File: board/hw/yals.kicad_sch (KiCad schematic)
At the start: 2 parts, among them J2 UART

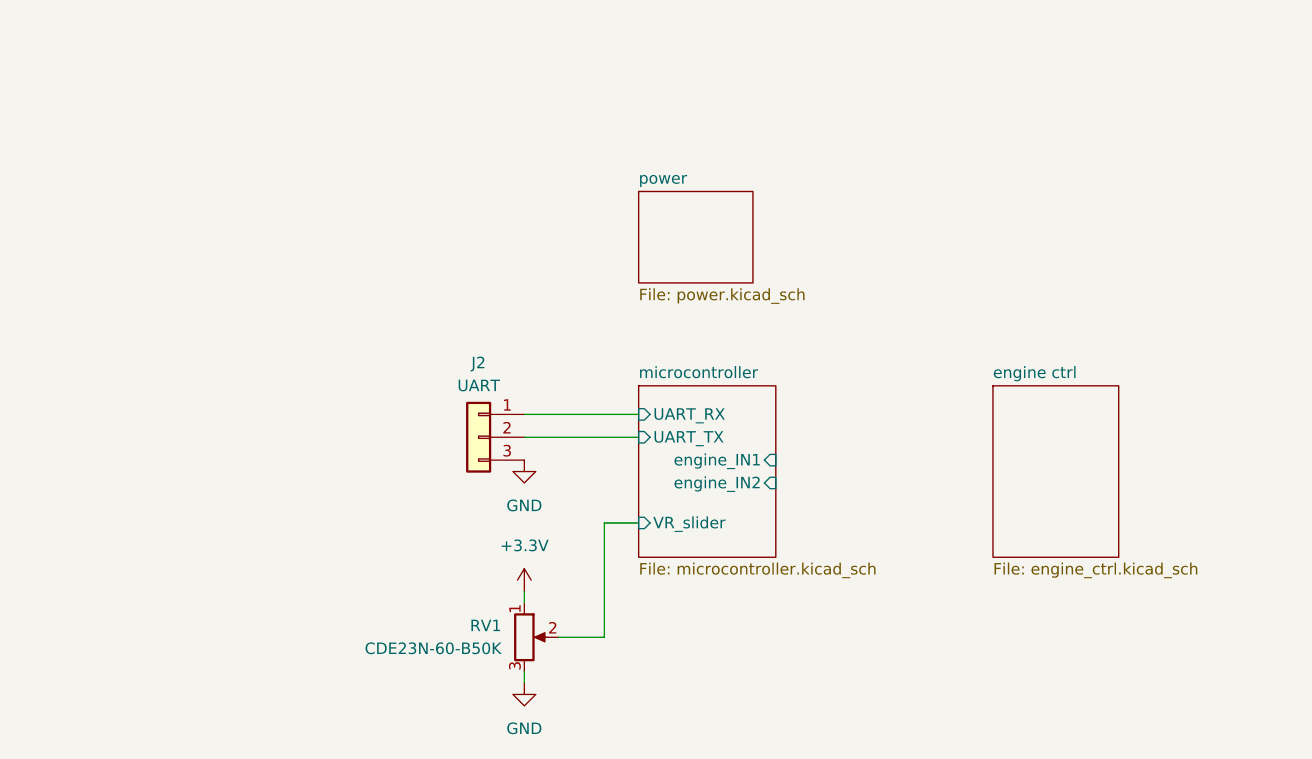
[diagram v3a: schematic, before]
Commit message: * moved potentiometer to engine's sheet * added engine's Vcc feedback
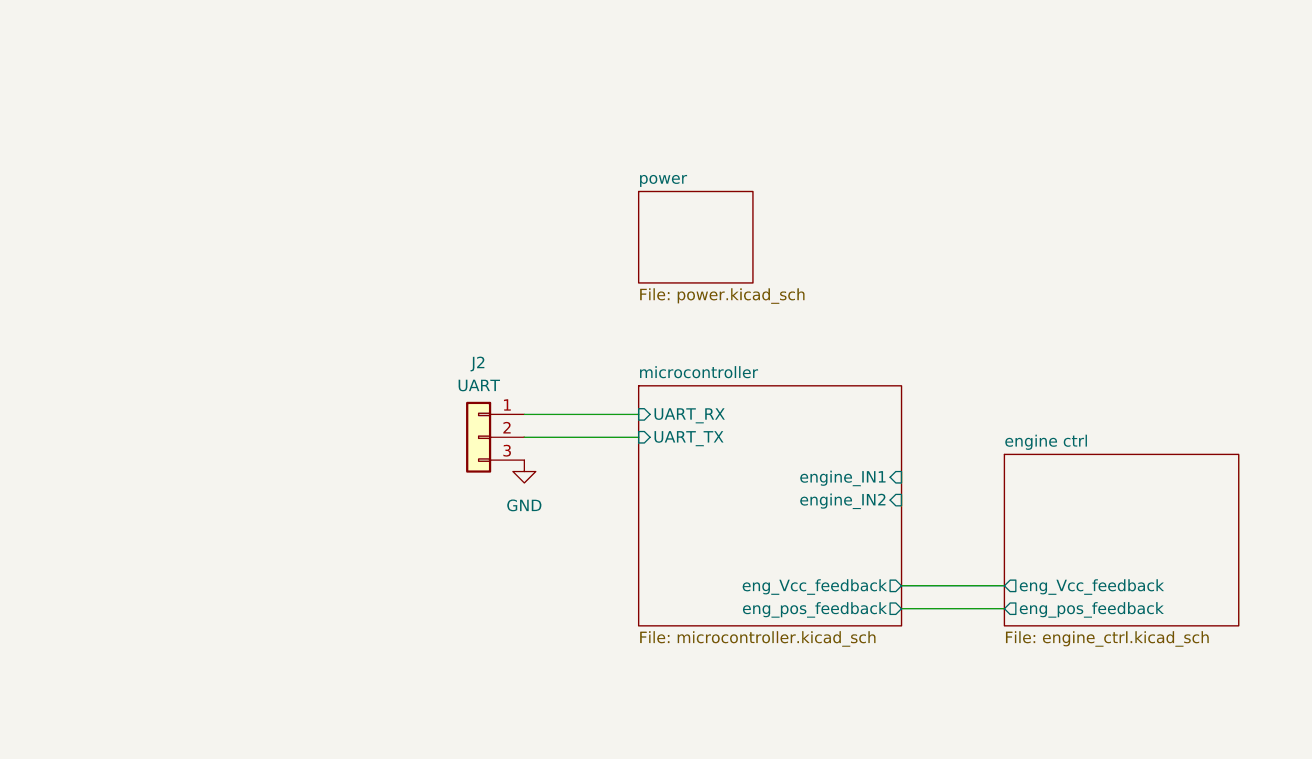
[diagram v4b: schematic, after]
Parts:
- removed RV1: CDE23N-60-B50K, st_passives_potentiometers:CDE23N-60-B50K, symbol Device:R_Potentiometer
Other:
- sheet engine ctrl ports: added eng_Vcc_feedback, eng_pos_feedback; removed none
- sheet microcontroller ports: added eng_Vcc_feedback, eng_pos_feedback; removed VR_slider
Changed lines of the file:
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@@
 (kicad_sch (version 20230121) (generator eeschema)
   (paper "A4")
-  (wire (pts (xy 109.22 107.95) (xy 109.22 109.22))
-    (stroke (width 0) (type default))
-  )
-  (wire (pts (xy 118.11 113.03) (xy 118.11 100.33))
-    (stroke (width 0) (type default))
-  )
-  (wire (pts (xy 109.22 116.84) (xy 109.22 118.11))
-    (stroke (width 0) (type default))
-  )
   (wire (pts (xy 109.22 90.805) (xy 121.92 90.805))
     (stroke (width 0) (type default))
   )
-  (wire (pts (xy 113.03 113.03) (xy 118.11 113.03))
+  (wire (pts (xy 151.13 109.855) (xy 162.56 109.855))
     (stroke (width 0) (type default))
   )
@@
     (stroke (width 0) (type default))
   )
-  (wire (pts (xy 118.11 100.33) (xy 121.92 100.33))
+  (wire (pts (xy 151.13 107.315) (xy 162.56 107.315))
     (stroke (width 0) (type default))
   )
@@
         (path "/920838ab-42d6-4f6a-a4ed-bf4606dd42d5"
           (reference "#PWR037") (unit 1)
-        )
-      )
-    )
-  )
-  (symbol (lib_id "Device:R_Potentiometer") (at 109.22 113.03 0) (unit 1)
-    (in_bom yes) (on_board yes) (dnp no) (fields_autoplaced)
-    (property "Reference" "RV1" (at 106.68 111.76 0)
-      (effects (font (size 1.27 1.27)) (justify right))
-    )
-    (property "Value" "CDE23N-60-B50K" (at 106.68 114.3 0)
-      (effects (font (size 1.27 1.27)) (justify right))
-    )
-    (property "Footprint" "st_passives_potentiometers:CDE23N-60-B50K" (at 109.22 113.03 0)
-      (effects (font (size 1.27 1.27)) hide)
-    )
-    (property "Datasheet" "~" (at 109.22 113.03 0)
-      (effects (font (size 1.27 1.27)) hide)
-    )
-    (pin "1")
-    (pin "3")
-    (pin "2")
-    (instances
-      (project "yals"
-        (path "/920838ab-42d6-4f6a-a4ed-bf4606dd42d5"
-          (reference "RV1") (unit 1)
-        )
-      )
-    )
-  )
-  (symbol (lib_id "power:GND") (at 109.22 118.11 0) (unit 1)
-    (in_bom yes) (on_board yes) (dnp no) (fields_autoplaced)
-    (property "Reference" "#PWR06" (at 109.22 124.46 0)
-      (effects (font (size 1.27 1.27)) hide)
-    )
-    (property "Value" "GND" (at 109.22 123.19 0)
-      (effects (font (size 1.27 1.27)))
-    )
-    (property "Footprint" "" (at 109.22 118.11 0)
-      (effects (font (size 1.27 1.27)) hide)
-    )
-    (property "Datasheet" "" (at 109.22 118.11 0)
-      (effects (font (size 1.27 1.27)) hide)
-    )
-    (pin "1")
-    (instances
-      (project "yals"
-        (path "/920838ab-42d6-4f6a-a4ed-bf4606dd42d5"
-          (reference "#PWR06") (unit 1)
-        )
-      )
-    )
-  )
-  (symbol (lib_id "power:+3.3V") (at 109.22 107.95 0) (unit 1)
-    (in_bom yes) (on_board yes) (dnp no) (fields_autoplaced)
-    (property "Reference" "#PWR07" (at 109.22 111.76 0)
-      (effects (font (size 1.27 1.27)) hide)
-    )
-    (property "Value" "+3.3V" (at 109.22 102.87 0)
-      (effects (font (size 1.27 1.27)))
-    )
-    (property "Footprint" "" (at 109.22 107.95 0)
-      (effects (font (size 1.27 1.27)) hide)
-    )
-    (property "Datasheet" "" (at 109.22 107.95 0)
-      (effects (font (size 1.27 1.27)) hide)
-    )
-    (pin "1")
-    (instances
-      (project "yals"
-        (path "/920838ab-42d6-4f6a-a4ed-bf4606dd42d5"
-          (reference "#PWR07") (unit 1)
         )
       )
@@
     )
   )
-  (sheet (at 121.92 85.09) (size 15.24 19.05) (fields_autoplaced)
+  (sheet (at 121.92 85.09) (size 29.21 26.67) (fields_autoplaced)
     (stroke (width 0.1524) (type solid))
     (fill (color 0 0 0 0.0000))
@@
       (effects (font (size 1.27 1.27)) (justify left bottom))
     )
-    (property "Sheetfile" "microcontroller.kicad_sch" (at 121.92 104.7246 0)
+    (property "Sheetfile" "microcontroller.kicad_sch" (at 121.92 112.3446 0)
       (effects (font (size 1.27 1.27)) (justify left top))
-    )
-    (pin "VR_slider" input (at 121.92 100.33 180)
-      (effects (font (size 1.27 1.27)) (justify left))
     )
     (pin "UART_RX" input (at 121.92 88.265 180)
@@
       (effects (font (size 1.27 1.27)) (justify left))
     )
-    (pin "engine_IN1" input (at 137.16 93.345 0)
+    (pin "engine_IN1" input (at 151.13 95.25 0)
       (effects (font (size 1.27 1.27)) (justify right))
     )
-    (pin "engine_IN2" input (at 137.16 95.885 0)
+    (pin "engine_IN2" input (at 151.13 97.79 0)
+      (effects (font (size 1.27 1.27)) (justify right))
+    )
+    (pin "eng_pos_feedback" output (at 151.13 109.855 0)
+      (effects (font (size 1.27 1.27)) (justify right))
+    )
+    (pin "eng_Vcc_feedback" output (at 151.13 107.315 0)
       (effects (font (size 1.27 1.27)) (justify right))
     )
@@
     )
   )
-  (sheet (at 161.29 85.09) (size 13.97 19.05) (fields_autoplaced)
+  (sheet (at 162.56 92.71) (size 26.035 19.05) (fields_autoplaced)
     (stroke (width 0.1524) (type solid))
     (fill (color 0 0 0 0.0000))
-    (property "Sheetname" "engine ctrl" (at 161.29 84.3784 0)
+    (property "Sheetname" "engine ctrl" (at 162.56 91.9984 0)
       (effects (font (size 1.27 1.27)) (justify left bottom))
     )
-    (property "Sheetfile" "engine_ctrl.kicad_sch" (at 161.29 104.7246 0)
+    (property "Sheetfile" "engine_ctrl.kicad_sch" (at 162.56 112.3446 0)
       (effects (font (size 1.27 1.27)) (justify left top))
     )
+    (pin "eng_pos_feedback" output (at 162.56 109.855 180)
+      (effects (font (size 1.27 1.27)) (justify left))
+    )
+    (pin "eng_Vcc_feedback" output (at 162.56 107.315 180)
+      (effects (font (size 1.27 1.27)) (justify left))
+    )
     (instances

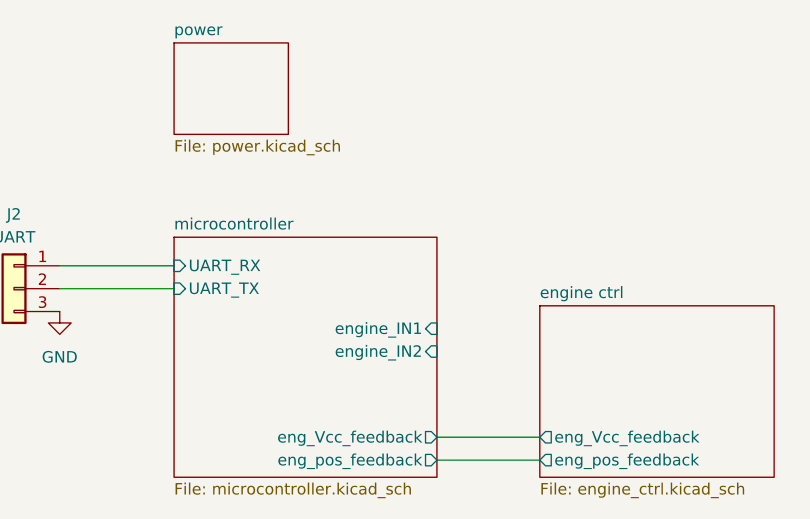
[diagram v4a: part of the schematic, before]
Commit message: added engine driver with votage measuring resistor to schematics
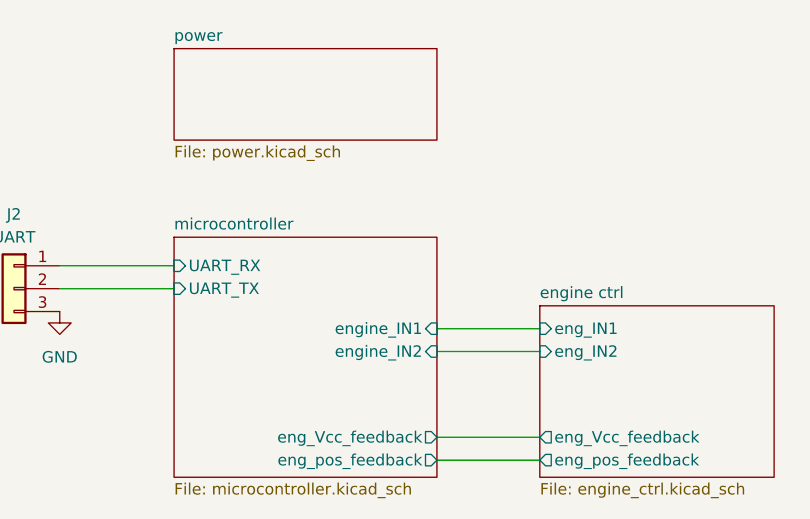
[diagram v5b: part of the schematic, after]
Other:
- sheet engine ctrl ports: added eng_IN1, eng_IN2; removed none
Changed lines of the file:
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@@
+    (stroke (width 0) (type default))
+  )
+  (wire (pts (xy 151.13 97.79) (xy 162.56 97.79))
     (stroke (width 0) (type default))
   )
@@
   )
   (wire (pts (xy 109.22 88.265) (xy 121.92 88.265))
+    (stroke (width 0) (type default))
+  )
+  (wire (pts (xy 151.13 95.25) (xy 162.56 95.25))
     (stroke (width 0) (type default))
   )
@@
     )
   )
-  (sheet (at 121.92 63.5) (size 12.7 10.16) (fields_autoplaced)
+  (sheet (at 121.92 64.135) (size 29.21 10.16) (fields_autoplaced)
     (stroke (width 0.1524) (type solid))
     (fill (color 0 0 0 0.0000))
-    (property "Sheetname" "power" (at 121.92 62.7884 0)
+    (property "Sheetname" "power" (at 121.92 63.4234 0)
       (effects (font (size 1.27 1.27)) (justify left bottom))
     )
-    (property "Sheetfile" "power.kicad_sch" (at 121.92 74.2446 0)
+    (property "Sheetfile" "power.kicad_sch" (at 121.92 74.8796 0)
       (effects (font (size 1.27 1.27)) (justify left top))
     )
@@
       (effects (font (size 1.27 1.27)) (justify left))
     )
+    (pin "eng_IN1" input (at 162.56 95.25 180)
+      (effects (font (size 1.27 1.27)) (justify left))
+    )
+    (pin "eng_IN2" input (at 162.56 97.79 180)
+      (effects (font (size 1.27 1.27)) (justify left))
+    )

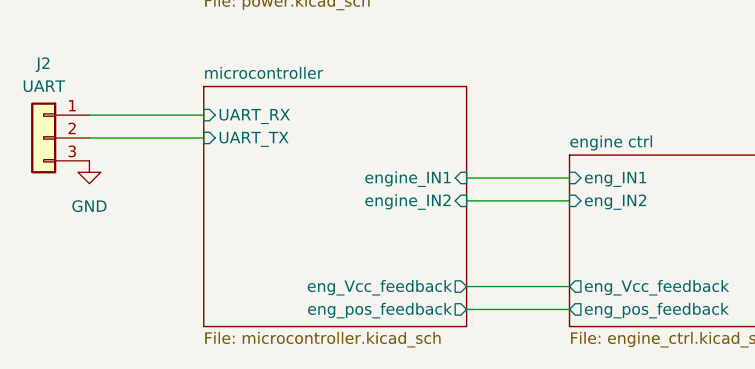
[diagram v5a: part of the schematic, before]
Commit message: fixed feedback pins directions
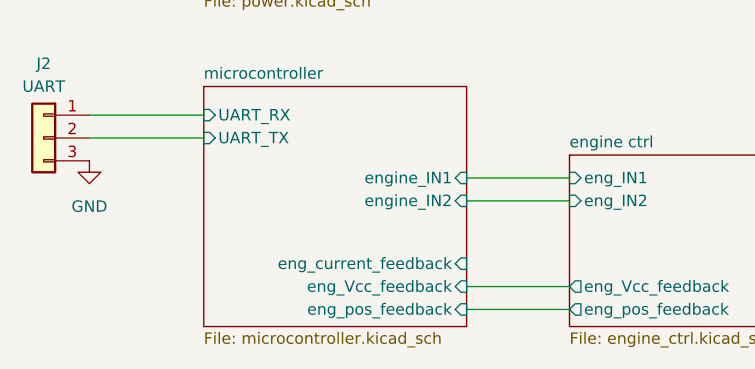
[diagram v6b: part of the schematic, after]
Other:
- sheet microcontroller ports: added eng_current_feedback; removed none
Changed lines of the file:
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@@
       (effects (font (size 1.27 1.27)) (justify right))
     )
-    (pin "eng_pos_feedback" output (at 151.13 109.855 0)
+    (pin "eng_pos_feedback" input (at 151.13 109.855 0)
       (effects (font (size 1.27 1.27)) (justify right))
     )
-    (pin "eng_Vcc_feedback" output (at 151.13 107.315 0)
+    (pin "eng_Vcc_feedback" input (at 151.13 107.315 0)
       (effects (font (size 1.27 1.27)) (justify right))
     )
+    (pin "eng_current_feedback" input (at 151.13 104.775 0)
+      (effects (font (size 1.27 1.27)) (justify right))
+    )
